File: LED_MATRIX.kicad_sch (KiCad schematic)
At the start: 0 parts

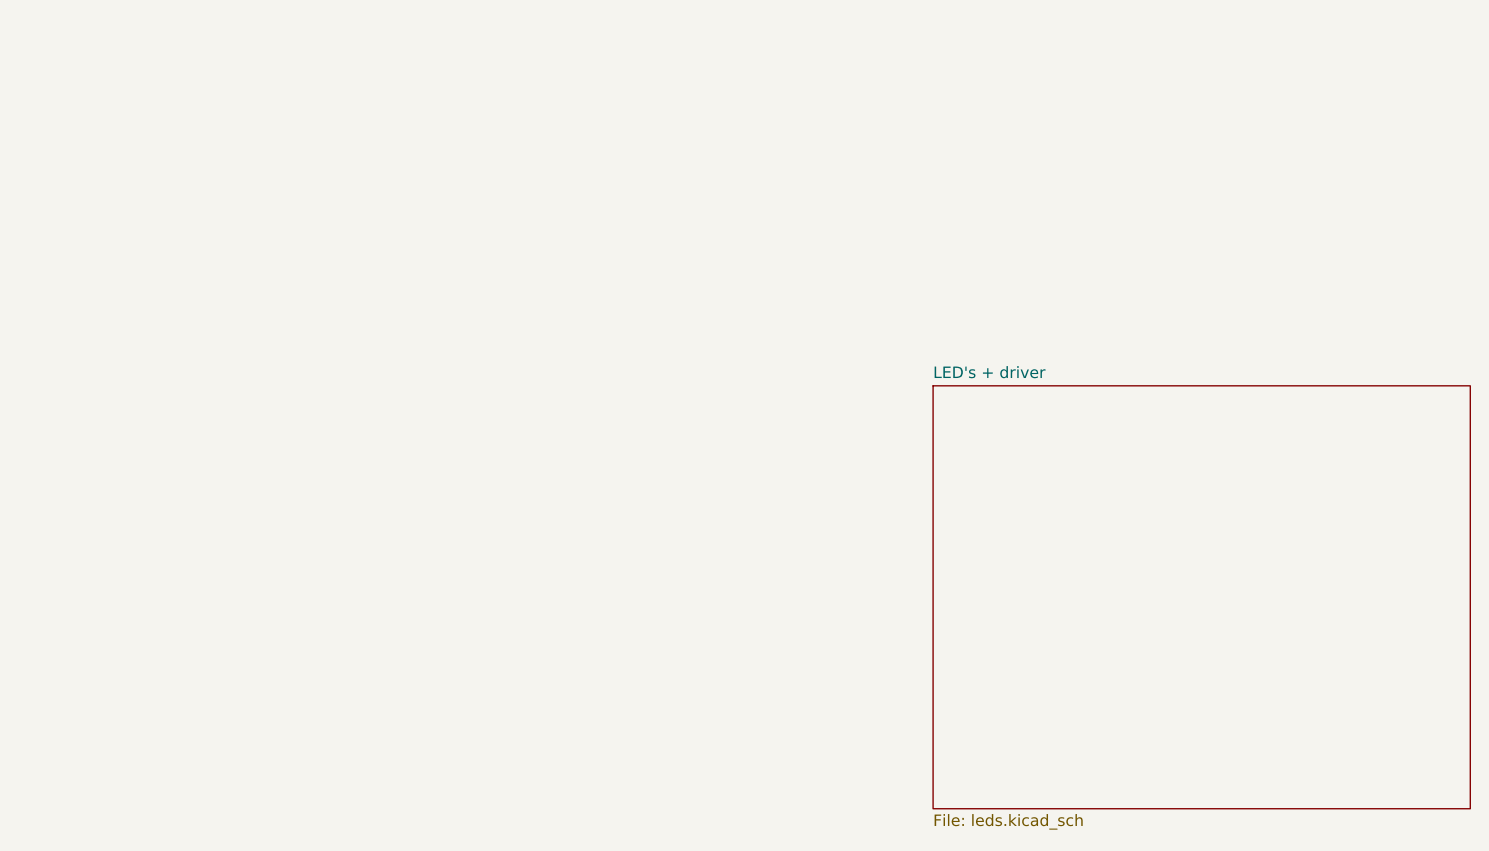
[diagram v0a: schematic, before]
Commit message: Added the led driver chip and connected all the pins
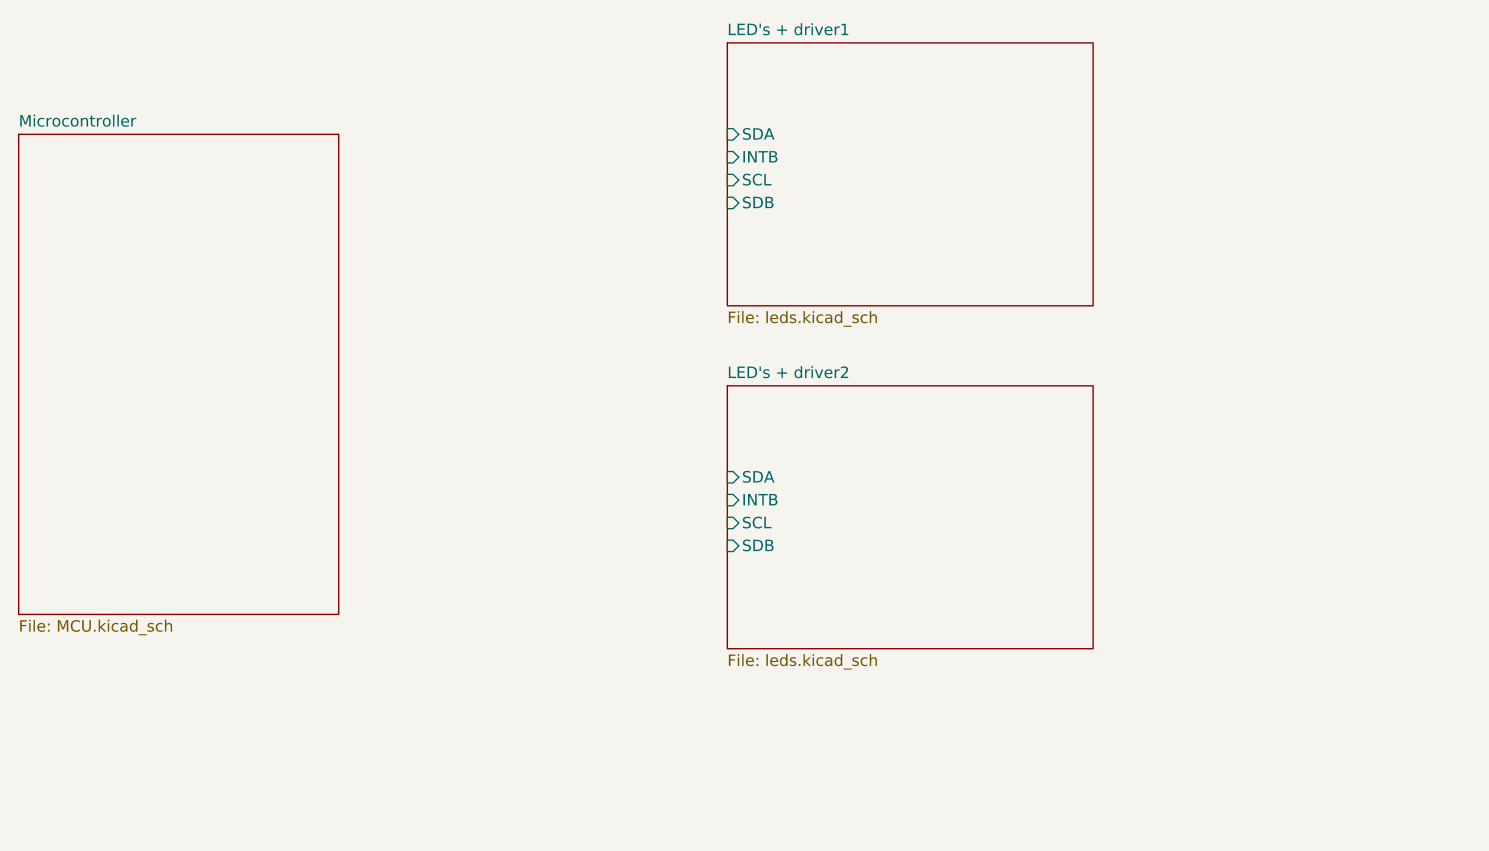
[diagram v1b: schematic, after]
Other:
- sheet LED's + driver renamed LED's + driver2
- added sheet LED's + driver1 (leds.kicad_sch)
- added sheet Microcontroller (MCU.kicad_sch)
- sheet LED's + driver2 ports: added INTB, SCL, SDA, SDB; removed none
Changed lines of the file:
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@@
 (kicad_sch (version 20230121) (generator eeschema)
   (paper "A4")
-  (sheet (at 195.58 104.14) (size 59.69 46.99) (fields_autoplaced)
+  (sheet (at 172.72 104.14) (size 40.64 29.21) (fields_autoplaced)
     (stroke (width 0.1524) (type solid))
     (fill (color 0 0 0 0.0000))
-    (property "Sheetname" "LED's + driver" (at 195.58 103.4284 0)
+    (property "Sheetname" "LED's + driver2" (at 172.72 103.4284 0)
       (effects (font (size 1.27 1.27)) (justify left bottom))
     )
-    (property "Sheetfile" "leds.kicad_sch" (at 195.58 151.7146 0)
+    (property "Sheetfile" "leds.kicad_sch" (at 172.72 133.9346 0)
       (effects (font (size 1.27 1.27)) (justify left top))
+    )
+    (pin "SDA" input (at 172.72 114.3 180)
+      (effects (font (size 1.27 1.27)) (justify left))
+    )
+    (pin "INTB" input (at 172.72 116.84 180)
+      (effects (font (size 1.27 1.27)) (justify left))
+    )
+    (pin "SCL" input (at 172.72 119.38 180)
+      (effects (font (size 1.27 1.27)) (justify left))
+    )
+    (pin "SDB" input (at 172.72 121.92 180)
+      (effects (font (size 1.27 1.27)) (justify left))
     )
     (instances
@@
       )
     )
+  )
+  (sheet (at 172.72 66.04) (size 40.64 29.21) (fields_autoplaced)
+    (stroke (width 0.1524) (type solid))
+    (fill (color 0 0 0 0.0000))
+    (property "Sheetname" "LED's + driver1" (at 172.72 65.3284 0)
+      (effects (font (size 1.27 1.27)) (justify left bottom))
+    )
+    (property "Sheetfile" "leds.kicad_sch" (at 172.72 95.8346 0)
+      (effects (font (size 1.27 1.27)) (justify left top))
+    )
+    (pin "SDA" input (at 172.72 76.2 180)
+      (effects (font (size 1.27 1.27)) (justify left))
+    )
+    (pin "INTB" input (at 172.72 78.74 180)
+      (effects (font (size 1.27 1.27)) (justify left))
+    )
+    (pin "SCL" input (at 172.72 81.28 180)
+      (effects (font (size 1.27 1.27)) (justify left))
+    )
+    (pin "SDB" input (at 172.72 83.82 180)
+      (effects (font (size 1.27 1.27)) (justify left))
+    )
+    (instances
+      (project "LED_MATRIX"
+        (path "/ceb06db9-8f49-4de4-b9ca-5fa52e791f62" (page "3"))
+      )
+    )
+  )
+  (sheet (at 93.98 76.2) (size 35.56 53.34) (fields_autoplaced)
+    (stroke (width 0.1524) (type solid))
+    (fill (color 0 0 0 0.0000))
+    (property "Sheetname" "Microcontroller" (at 93.98 75.4884 0)
+      (effects (font (size 1.27 1.27)) (justify left bottom))
+    )
+    (property "Sheetfile" "MCU.kicad_sch" (at 93.98 130.1246 0)
+      (effects (font (size 1.27 1.27)) (justify left top))
+    )
+    (instances
+      (project "LED_MATRIX"
+        (path "/ceb06db9-8f49-4de4-b9ca-5fa52e791f62" (page "4"))
+      )
+    )
